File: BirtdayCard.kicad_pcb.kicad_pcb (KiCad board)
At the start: 2 copper layers, 150 x 150 mm, 56 parts, among them J1 Conn_01x04_Socket, J2 Conn_01x05_Pin, Q1 2N7002_C306856, U1 ESP32-C3-WROOM-02-N4(4MB), U2 AMS1117-3.3_C347222

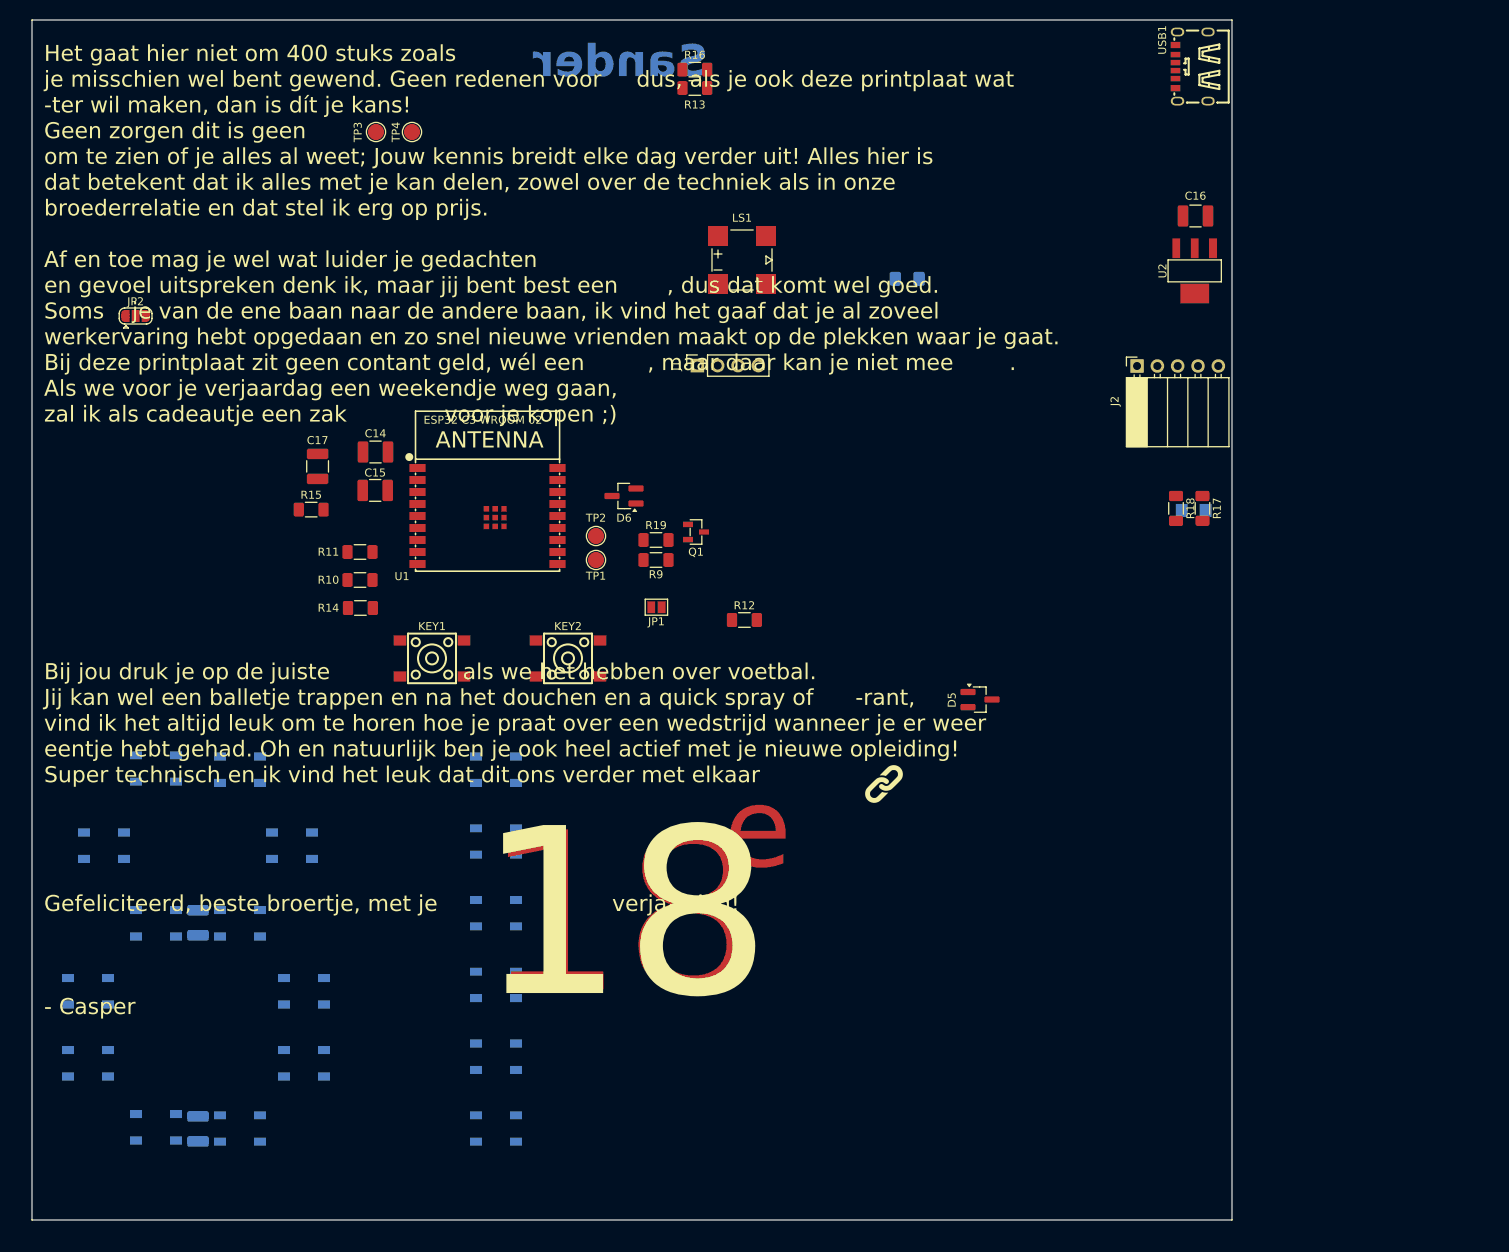
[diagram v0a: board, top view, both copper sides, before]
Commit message: Improved silkscreen and text
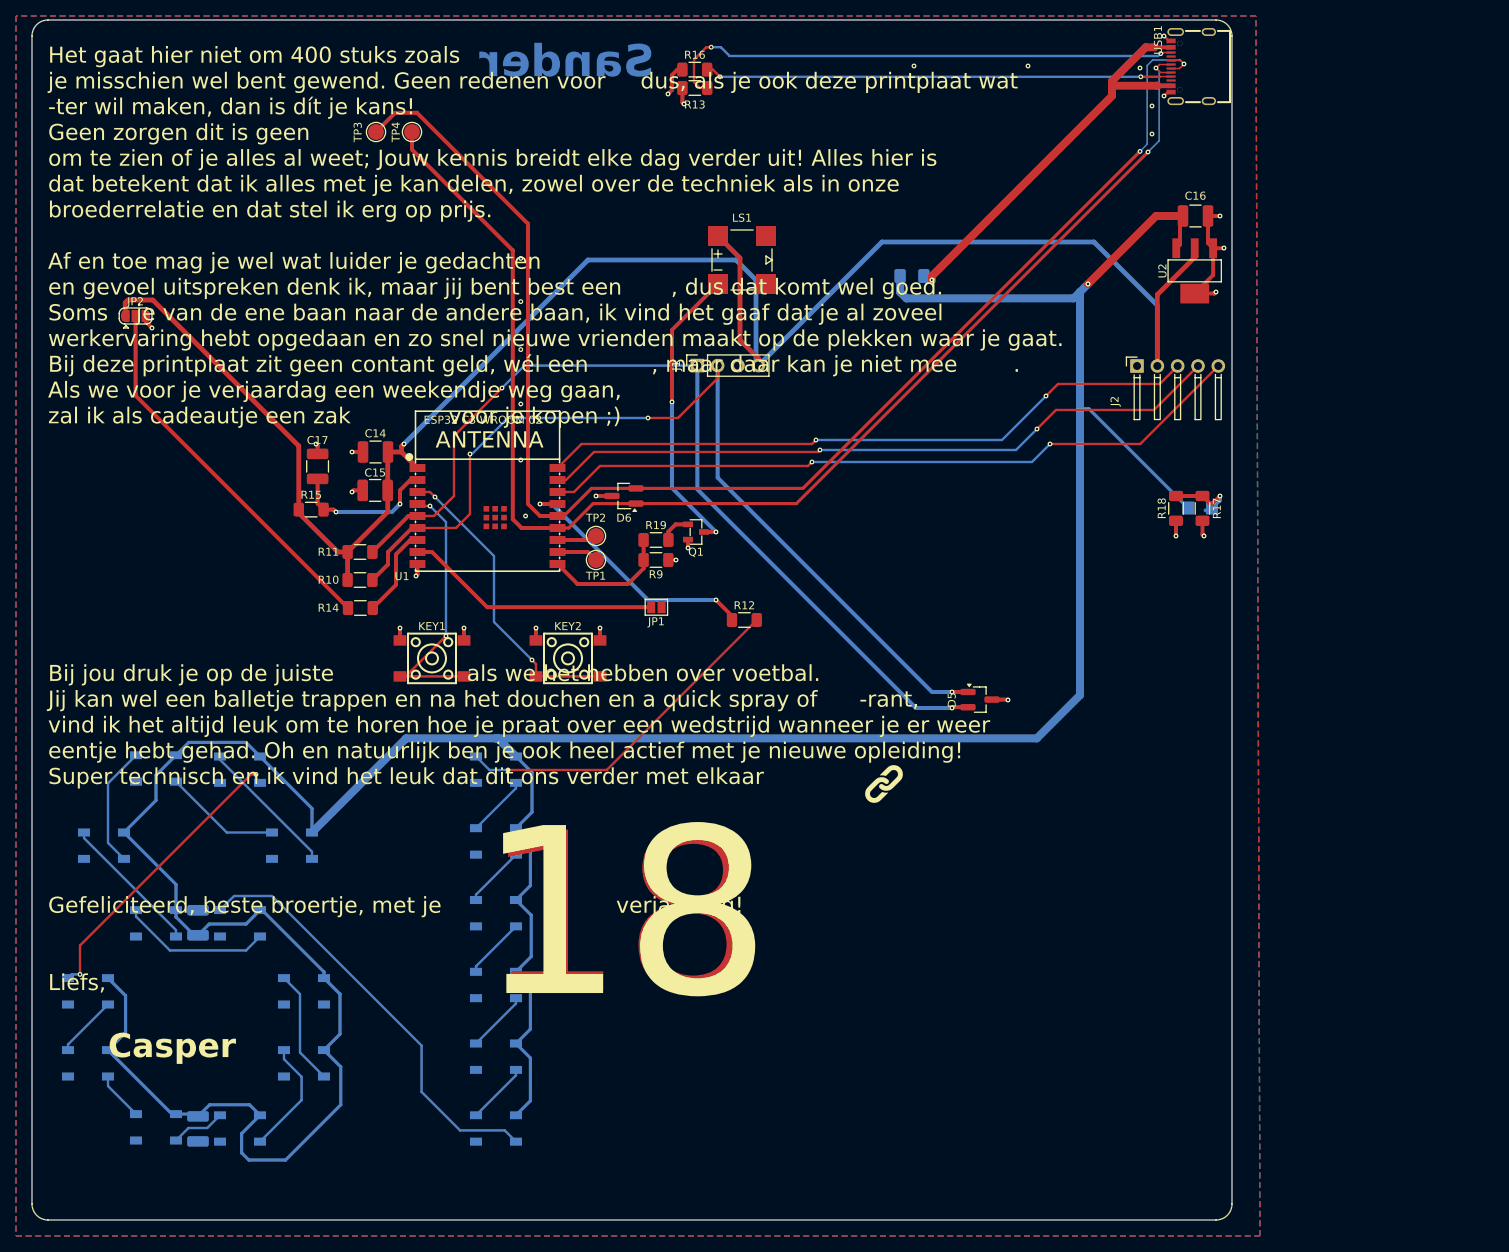
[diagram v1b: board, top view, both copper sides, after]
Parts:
- USB1: value TYPE-C 6P(073) -> TYPE-C16PIN; footprint easyeda2kicad:TYPE-C-SMD_TYPE-C-6P_5 -> easyeda2kicad:USB-C-SMD_TYPE-C16PIN
- moved LED2 0.85 mm to (170.5, 89.0)
- moved F1 0.69 mm to (134.5, 60.0)
- moved USB1 0.22 mm to (169.2, 33.8)
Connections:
- C32 pad 1: +3V3 -> +5V
- C33 pad 1: +3V3 -> +5V
- D10 pad 1: +3V3 -> +5V
- D11 pad 1: +3V3 -> +5V
- D12 pad 1: +3V3 -> +5V
- D13 pad 1: +3V3 -> +5V
- D14 pad 1: +3V3 -> +5V
- D15 pad 1: +3V3 -> +5V
- D16 pad 1: +3V3 -> +5V
- D17 pad 1: +3V3 -> +5V
- D18 pad 1: +3V3 -> +5V
- D19 pad 1: +3V3 -> +5V
- D20 pad 1: +3V3 -> +5V
- D21 pad 1: +3V3 -> +5V
- D22 pad 1: +3V3 -> +5V
- D23 pad 1: +3V3 -> +5V
- D24 pad 1: +3V3 -> +5V
- D25 pad 1: +3V3 -> +5V
- D26 pad 1: +3V3 -> +5V
- D27 pad 1: +3V3 -> +5V
- J2 pad 3: GPIO2 -> GPIO0
- J2 pad 5: GPIO0 -> GPIO2
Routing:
- net +5V: track 0.00 -> 437.5 mm, vias 0 -> 1
- net +3V3: track 0.00 -> 238.7 mm, vias 0 -> 1
- net D+_USB: track 0.00 -> 176.6 mm, vias 0 -> 2
- net D-_USB: track 0.00 -> 168.4 mm, vias 0 -> 2
- net GPIO7: track 0.00 -> 116.9 mm, vias 0 -> 3
- net GPIO6: track 0.00 -> 115.3 mm, vias 0 -> 2
- net GPIO2: track 0.00 -> 89.1 mm, vias 0 -> 2
- net GPIO1: track 0.00 -> 86.0 mm, vias 0 -> 2
- net GPIO0: track 0.00 -> 82.8 mm, vias 0 -> 2
- net Net-(USB1-CC2): track 0.00 -> 65.7 mm, vias 0 -> 2
- net Net-(USB1-CC1): track 0.00 -> 58.4 mm, vias 0 -> 2
- net Net-(D15-DOUT): track 0.00 -> 53.8 mm
- net Net-(F1-Pad1): track 0.00 -> 52.3 mm, vias 0 -> 1
- net GND: track 0.00 -> 48.6 mm, vias 0 -> 32
- net Net-(JP2-C): track 0.00 -> 47.5 mm
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- added copper zone on B.Cu, net GND
- added copper zone on F.Cu, net GND
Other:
- outline, holes or cut-outs redrawn
- board text added: "Casper"
- board text added: "Wauw, 18 jaar oud! Nu ben je officieel volwassen, wat betekent dat je allemaal nieuwe features hebt unlocked in de gezamenlijke server. Even op een rijtje: 1. Full access to the worldmap 2. Een eigen stem (waar misschien naar wordt geluisterd!) 3. Je eigen zorgver én andere vaste lasten! 4. Toegang tot de vierwielige fatbike crusher (nadat je je plastic kaartje hebt gescoord) 5. Gratis onderdak, 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"
- board text removed: "Wauw, 18 jaar oud! Nu ben je officieel volwassen, wat betekent dat je allemaal nieuwe features hebt unlocked in de gezamenlijke server. Even op een rijtje: 1. Full access to the worldmap 2. Een eigen stem (waar misschien naar wordt geluisterd!) 3. Je eigen zorgver én andere vaste lasten! 4. Toegang tot de vierwielige fatbike crusher (wanneer je je plastic kaartje hebt gescoord) 5. Gratis onderdak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"

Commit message: Updated schematic and PCB (resistor removed)
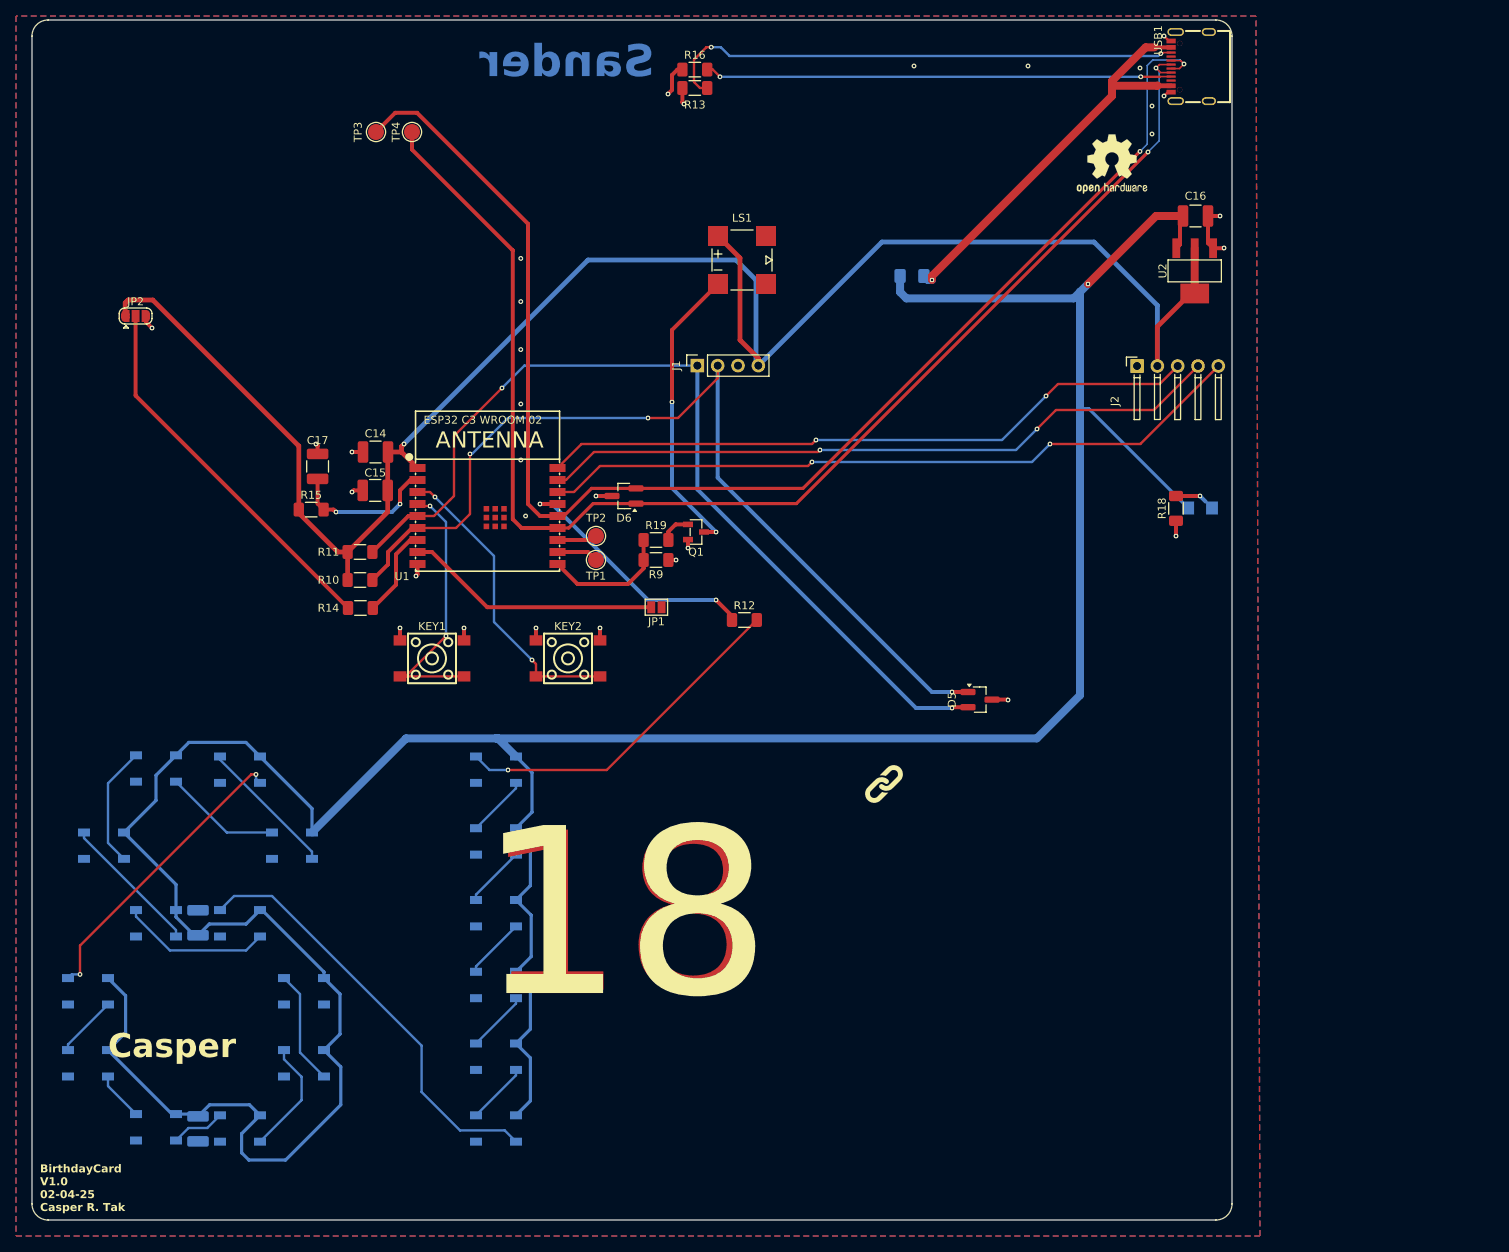
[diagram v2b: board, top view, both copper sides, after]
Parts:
- removed R17: 1k, Resistor_SMD:R_1206_3216Metric_Pad1.30x1.75mm_HandSolder
- added REF**: OSHW-Logo2_9.8x8mm_SilkScreen, Symbol:OSHW-Logo2_9.8x8mm_SilkScreen, F.Cu at (159.5, 46.0)
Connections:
- U2 pad 4: GND -> +3V3
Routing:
- net GND: track 48.6 -> 37.3 mm, vias 32 -> 30
- net Net-(LED2-K): track 9.17 -> 3.99 mm
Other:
- board text added: "BirthdayCard V1.0 02-04-25 Casper R. Tak"
- board text added: "Wauw, 18 jaar oud! Nu ben je officieel volwassen, wat betekent dat je allemaal nieuwe features hebt unlocked in de gezamenlijke server. Even op een rijtje: 1. Full access to the worldmap 2. Een eigen stem (waar misschien ook naar wordt geluisterd) 3. Je eigen zorgver én andere vaste lasten! 4. Toegang tot de vierwielige fatbike crusher (nadat je dat plastic kaartje hebt gescoord) 5. Gratis onderd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"
- board text removed: "Het gaat hier niet om 400 stuks zoals je misschien wel bent gewend. Geen redenen voor dus, als je ook deze printplaat wat -ter wil maken, dan is dít je kans! Geen zorgen dit is geen om te zien of je alles al weet; Jouw kennis breidt elke dag verder uit! Alles hier is dat betekent dat ik alles met je kan delen, zowel over de techniek als in onze broederrelatie en dat stel ik erg op prijs. Af en to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"
- board text removed: "Wauw, 18 jaar oud! Nu ben je officieel volwassen, wat betekent dat je allemaal nieuwe features hebt unlocked in de gezamenlijke server. Even op een rijtje: 1. Full access to the worldmap 2. Een eigen stem (waar misschien naar wordt geluisterd!) 3. Je eigen zorgver én andere vaste lasten! 4. Toegang tot de vierwielige fatbike crusher (nadat je je plastic kaartje hebt gescoord) 5. Gratis onderdak, 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"

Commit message: updated text
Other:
- board text added: "Het gaat hier niet om 400 stuks zoals je misschien wel bent gewend. Geen redenen voor dus, als je ook deze printplaat wat -ter wil maken, dan is dít je kans! Geen zorgen dit is geen om te zien of je alles al weet; Jouw kennis breidt elke dag verder uit! Alles hier is dat betekent dat ik alles met je kan delen, zowel over de techniek als in onze broederrelatie en dat stel ik erg op prijs. Af en to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"
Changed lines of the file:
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@@
+		)
+	)
+	(gr_text "Het gaat hier niet om 400 stuks zoals \nje misschien wel bent gewend. Geen redenen voor     dus, als je ook deze printplaat wat \n-ter wil maken, dan is dít je kans! \nGeen zorgen dit is geen  \nom te zien of je alles al weet; Jouw kennis breidt elke dag verder uit! Alles hier is  \ndat betekent dat ik alles met je kan delen, zowel over de techniek als in onze \nbroederrelatie en dat stel ik erg op prijs. \n\nAf en toe mag je wel wat luider je gedachten \nen gevoel uitspreken denk ik, maar jij bent best een       , dus dat komt wel goed. \nSoms    je van de ene naar de andere baan. Ik vind het gaaf dat je al zoveel \nwerkervaring hebt opgedaan en zo snel nieuwe vrienden maakt op de plekken waar je gaat. \nBij deze printplaat zit geen contant geld, wél een         , maar daar kan je niet mee        .\nAls we voor je verjaardag een weekendje weg gaan, \nzal ik als cadeautje een zak              voor je kopen ;) \n\n\n\n\n\n\n\n\n\nBij jou druk je op de juiste                   als we het gaan hebben over voetbal. \nJij kan wel een balletje trappen en na het douchen en a quick spray of      -rant, \nvind ik het altijd leuk om te horen hoe je praat over de wedstrijd wanneer je er weer \neen hebt gehad. Als laatste ben je ook heel druk met je nieuwe opleiding, lekker bezig,\nSuper technisch en ik vind het leuk dat dit ons verder met elkaar   \n\n\n\n\nGefeliciteerd, beste broertje, met je                         verjaardag! \n\n\nLiefs,\n"
+		(at 26.5 149.5 0)
+		(layer "F.SilkS")
+		(effects
+			(font
+				(size 2 2)
+				(thickness 0.25)
+			)
+			(justify left bottom)
 		)
 	)

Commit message: changed date
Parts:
- added REF**: KiCad-Logo2_12mm_SilkScreen, Symbol:KiCad-Logo2_12mm_SilkScreen, F.Cu at (158.0, 168.5)
- moved R18 15.6 mm to (157.5, 77.0), turned to 90 degrees
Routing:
- net Net-(LED2-K): track 3.99 -> 21.3 mm
